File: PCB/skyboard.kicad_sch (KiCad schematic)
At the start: 10 parts, among them SW1 SW_Push, SW2 SW_Push, SW3 SW_Push, SW4 SW_Push, SW5 SW_Push, SW6 SW_Push, SW7 RotaryEncoder_Switch, U1 XIAO-RP2040-DIP

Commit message: Added ground to the LEDs
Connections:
- net +5V: now also D1.4 (VDD), D2.4 (VDD)
- net GND: now also D1.2 (VSS), D2.2 (VSS), SW7.C
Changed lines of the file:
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@@
+	)
+	(junction
+		(at 186.69 50.8)
+		(diameter 0)
+		(color 0 0 0 0)
 	)
 	(junction
@@
 					(unit 1)
 				)
+			)
+		)
+	)
+	(symbol
+		(lib_id "power:+5V")
+		(at 186.69 50.8 0)
+		(unit 1)
+		(exclude_from_sim no)
+		(in_bom yes)
+		(on_board yes)
+		(dnp no)
+		(fields_autoplaced yes)
+		(property "Reference" "#PWR05"
+			(at 186.69 54.61 0)
+			(effects
+				(font
+					(size 1.27 1.27)
+				)
+				(hide yes)
+			)
+		)
+		(property "Value" "+5V"
+			(at 186.69 45.72 0)
+			(effects
+				(font
+					(size 1.27 1.27)
+				)
+			)
+		)
+		(property "Footprint" ""
+			(at 186.69 50.8 0)
+			(effects
+				(font
+					(size 1.27 1.27)
+				)
+				(hide yes)
+			)
+		)
+		(property "Datasheet" ""
+			(at 186.69 50.8 0)
+			(effects
+				(font
+					(size 1.27 1.27)
+				)
+				(hide yes)
+			)
+		)
+		(property "Description" "Power symbol creates a global label with name \"+5V\""
+			(at 186.69 50.8 0)
+			(effects
+				(font
+					(size 1.27 1.27)
+				)
+				(hide yes)
+			)
+		)
+		(pin "1"
+		)
+		(instances
+			(project ""
+				(path "/937b10a8-9a30-472f-9ac2-a174a3cf71d1"
+					(reference "#PWR05")
+					(unit 1)
+				)
+			)
+		)
+	)
+	(symbol
+		(lib_id "power:GND")
+		(at 160.02 67.31 0)
+		(unit 1)
+		(exclude_from_sim no)
+		(in_bom yes)
+		(on_board yes)
+		(dnp no)
+		(fields_autoplaced yes)
+		(property "Reference" "#PWR04"
+			(at 160.02 73.66 0)
+			(effects
+				(font
+					(size 1.27 1.27)
+				)
+				(hide yes)
+			)
+		)
+		(property "Value" "GND"
+			(at 160.02 72.39 0)
+			(effects
+				(font
+					(size 1.27 1.27)
+				)
+			)
+		)
+		(property "Footprint" ""
+			(at 160.02 67.31 0)
+			(effects
+				(font
+					(size 1.27 1.27)
+				)
+				(hide yes)
+			)
+		)
+		(property "Datasheet" ""
+			(at 160.02 67.31 0)
+			(effects
+				(font
+					(size 1.27 1.27)
+				)
+				(hide yes)
+			)
+		)
+		(property "Description" "Power symbol creates a global label with name \"GND\" , ground"
+			(at 160.02 67.31 0)
+			(effects
+				(font
+					(size 1.27 1.27)
+				)
+				(hide yes)
+			)
+		)
+		(pin "1"
+		)
+		(instances
+			(project ""
+				(path "/937b10a8-9a30-472f-9ac2-a174a3cf71d1"
+					(reference "#PWR04")
+					(unit 1)
+				)

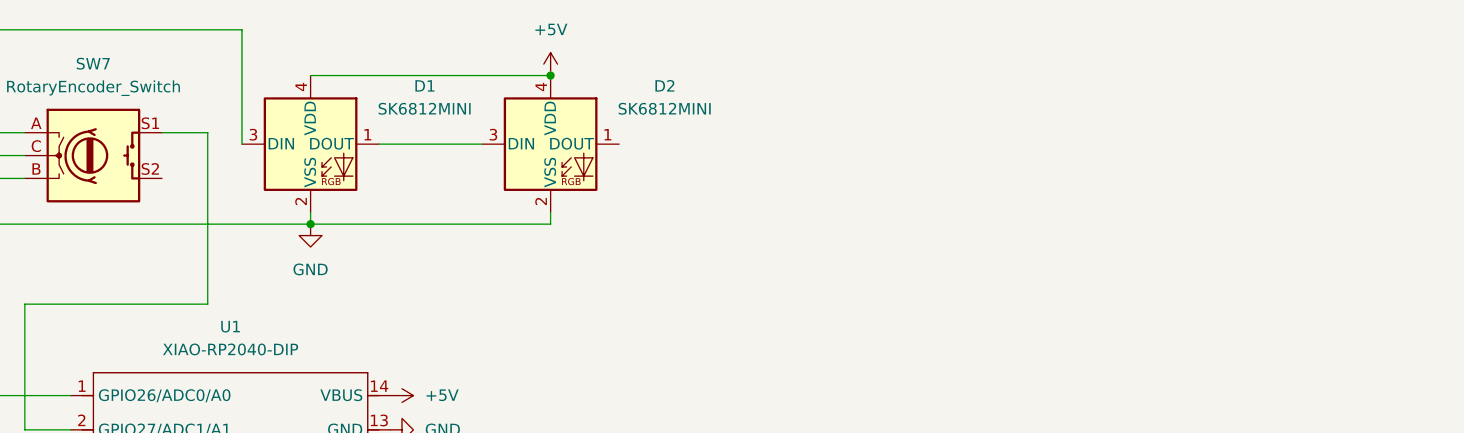
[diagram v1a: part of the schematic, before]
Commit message: Added extra LEDs under the switches, fixed wiring
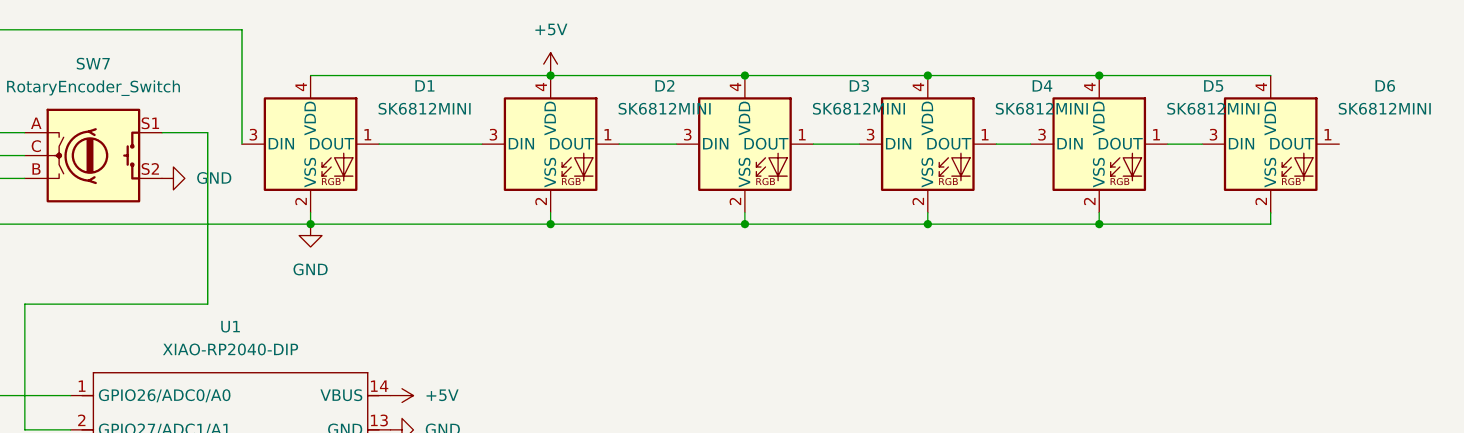
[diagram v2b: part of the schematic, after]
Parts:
- added D3, D4, D5, D6: SK6812MINI, Hackclub Footprints:MX_SK6812MINI-E_REV, symbol LED:SK6812MINI
- D1, D2: footprint LED_SMD:LED_SK6812MINI_PLCC4_3.5x3.5mm_P1.75mm -> Hackclub Footprints:MX_SK6812MINI-E_REV
- U1: footprint OPL:XIAO-RP2040-DIP -> Hackclub Footprints:XIAO-RP2040-DIP
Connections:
- net +5V: now also D3.4 (VDD), D4.4 (VDD), D5.4 (VDD), D6.4 (VDD)
- net GND: now also SW7.S2, D3.2 (VSS), D4.2 (VSS), D5.2 (VSS), D6.2 (VSS)
- net at D2.1 (DOUT): now also D3.3 (DIN)
- new net: D5.1 (DOUT), D6.3 (DIN)
- new net: D4.1 (DOUT), D5.3 (DIN)
- new net: D3.1 (DOUT), D4.3 (DIN)
